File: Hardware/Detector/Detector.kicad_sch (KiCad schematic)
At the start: 0 parts

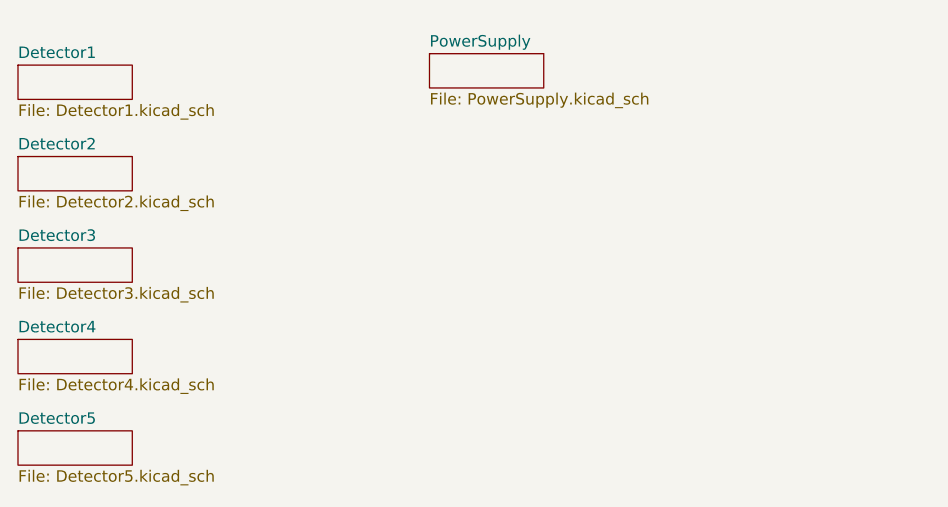
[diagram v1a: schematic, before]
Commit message: further implementation of low cost version
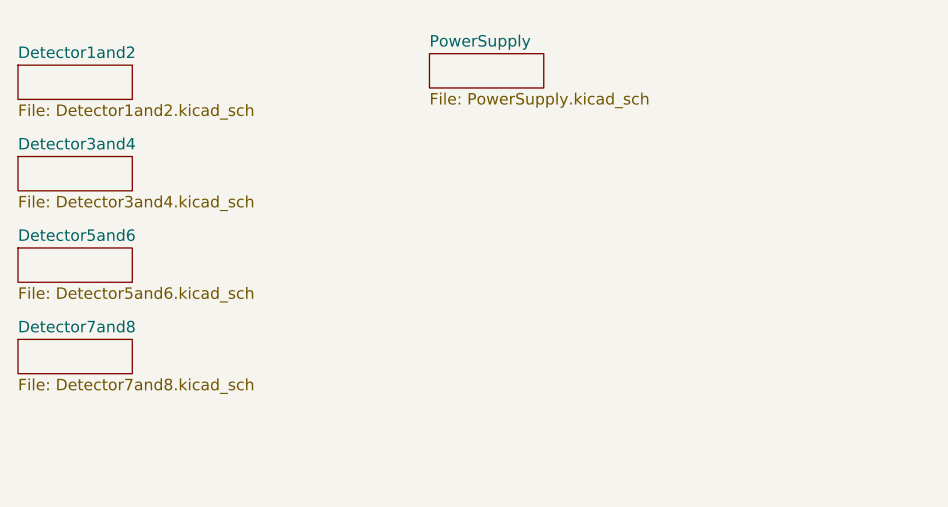
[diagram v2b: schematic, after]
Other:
- sheet Detector1 renamed Detector1and2
- sheet Detector2 renamed Detector3and4
- sheet Detector3 renamed Detector5and6
- sheet Detector4 renamed Detector7and8
- removed sheet Detector5
- sheet Detector1and2: file Detector1.kicad_sch -> Detector1and2.kicad_sch
- sheet Detector3and4: file Detector2.kicad_sch -> Detector3and4.kicad_sch
- sheet Detector5and6: file Detector3.kicad_sch -> Detector5and6.kicad_sch
- sheet Detector7and8: file Detector4.kicad_sch -> Detector7and8.kicad_sch

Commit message: fixed footprints, changed kicad scheet name, added a bit of decription to schematics
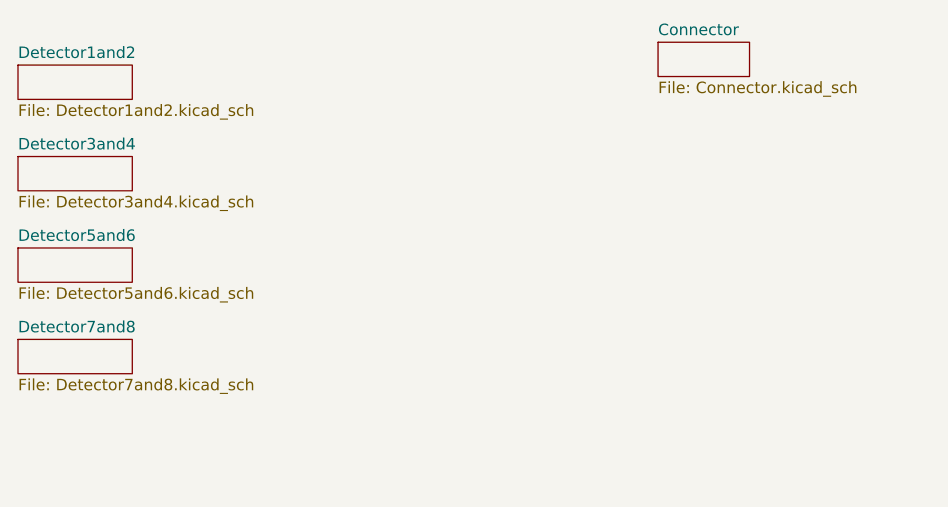
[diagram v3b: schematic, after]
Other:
- removed sheet PowerSupply
- added sheet Connector (Connector.kicad_sch)
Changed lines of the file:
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@@
 (kicad_sch (version 20210621) (generator eeschema)
   (paper "A4")
+  (sheet (at 132.08 43.18) (size 10.16 3.81) (fields_autoplaced)
+    (stroke (width 0.0006) (type solid) (color 0 0 0 0))
+    (fill (color 0 0 0 0.0000))
+    (property "Sheet name" "Connector" (id 0) (at 132.08 42.5443 0)
+      (effects (font (size 1.27 1.27)) (justify left bottom))
+    )
+    (property "Sheet file" "Connector.kicad_sch" (id 1) (at 132.08 47.4987 0)
+      (effects (font (size 1.27 1.27)) (justify left top))
+    )
+  )
   (sheet (at 60.96 45.72) (size 12.7 3.81) (fields_autoplaced)
     (stroke (width 0) (type solid) (color 0 0 0 0))
@@
     )
     (property "Sheet file" "Detector7and8.kicad_sch" (id 1) (at 60.96 80.5185 0)
-      (effects (font (size 1.27 1.27)) (justify left top))
-    )
-  )
-  (sheet (at 106.68 44.45) (size 12.7 3.81) (fields_autoplaced)
-    (stroke (width 0) (type solid) (color 0 0 0 0))
-    (fill (color 0 0 0 0.0000))
-    (property "Sheet name" "PowerSupply" (id 0) (at 106.68 43.8145 0)
-      (effects (font (size 1.27 1.27)) (justify left bottom))
-    )
-    (property "Sheet file" "PowerSupply.kicad_sch" (id 1) (at 106.68 48.7685 0)
       (effects (font (size 1.27 1.27)) (justify left top))
     )
@@
     (path "/00000000-0000-0000-0000-00006126c995" (page "4"))
     (path "/00000000-0000-0000-0000-00006126cbd6" (page "5"))
-    (path "/00000000-0000-0000-0000-0000613a12f3" (page "7"))
+    (path "/5f2e3474-4294-4ba3-9888-5e127036e05d" (page "7"))
   )
   (symbol_instances
@@
       (reference "#FLG01") (unit 1) (value "PWR_FLAG") (footprint "")
     )
-    (path "/00000000-0000-0000-0000-0000613a12f3/00000000-0000-0000-0000-0000613a2d09"
-      (reference "#FLG02") (unit 1) (value "PWR_FLAG") (footprint "")
-    )
-    (path "/00000000-0000-0000-0000-0000613a12f3/00000000-0000-0000-0000-0000613a2d03"
-      (reference "#FLG03") (unit 1) (value "PWR_FLAG") (footprint "")
-    )
-    (path "/00000000-0000-0000-0000-0000613a12f3/00000000-0000-0000-0000-0000613a2ce4"
-      (reference "#FLG04") (unit 1) (value "PWR_FLAG") (footprint "")
+    (path "/5f2e3474-4294-4ba3-9888-5e127036e05d/06133da6-7cc3-4082-a5f3-3c340855df19"
+      (reference "#FLG?") (unit 1) (value "PWR_FLAG") (footprint "")
+    )
+    (path "/5f2e3474-4294-4ba3-9888-5e127036e05d/853a2901-ebb3-4f30-bb7f-c3af7d416212"
+      (reference "#FLG?") (unit 1) (value "PWR_FLAG") (footprint "")
+    )
+    (path "/5f2e3474-4294-4ba3-9888-5e127036e05d/9d2454be-5e62-4368-82c6-b9619bf6d756"
+      (reference "#FLG?") (unit 1) (value "PWR_FLAG") (footprint "")
     )
     (path "/00000000-0000-0000-0000-00006126bc2d/00000000-0000-0000-0000-000061297e78"
@@
       (reference "#PWR019") (unit 1) (value "GND") (footprint "")
     )
-    (path "/00000000-0000-0000-0000-0000613a12f3/00000000-0000-0000-0000-0000613a2ceb"
-      (reference "#PWR020") (unit 1) (value "VCC") (footprint "")
-    )
-    (path "/00000000-0000-0000-0000-0000613a12f3/00000000-0000-0000-0000-0000613a2cf1"
-      (reference "#PWR021") (unit 1) (value "GND") (footprint "")
-    )
     (path "/00000000-0000-0000-0000-00006126bc2d/c606fb33-e83c-4379-997e-ae830a0633db"
       (reference "#PWR022") (unit 1) (value "GND") (footprint "")
@@
       (reference "#PWR026") (unit 1) (value "GND") (footprint "")
     )
+    (path "/5f2e3474-4294-4ba3-9888-5e127036e05d/c64404e3-c5a4-45e5-b3f5-f07ff96d3c86"
+      (reference "#PWR?") (unit 1) (value "GND") (footprint "")
+    )
+    (path "/5f2e3474-4294-4ba3-9888-5e127036e05d/f020742a-bb32-463f-a128-fd61cbeed9e0"
+      (reference "#PWR?") (unit 1) (value "VCC") (footprint "")
+    )
     (path "/00000000-0000-0000-0000-00006126bc2d/00000000-0000-0000-0000-000061297ddf"
       (reference "C1") (unit 1) (value "2p2") (footprint "Capacitor_SMD:C_0402_1005Metric")
@@
       (reference "R22") (unit 1) (value "10k") (footprint "Resistor_SMD:R_0402_1005Metric")
     )
-    (path "/00000000-0000-0000-0000-0000613a12f3/00000000-0000-0000-0000-00006158fd79"
-      (reference "TP1") (unit 1) (value "TestPoint") (footprint "TestPoint:TestPoint_THTPad_D2.5mm_Drill1.2mm")
-    )
-    (path "/00000000-0000-0000-0000-0000613a12f3/00000000-0000-0000-0000-0000615908a9"
-      (reference "TP2") (unit 1) (value "TestPoint") (footprint "TestPoint:TestPoint_THTPad_D2.5mm_Drill1.2mm")
-    )
-    (path "/00000000-0000-0000-0000-0000613a12f3/00000000-0000-0000-0000-000061592458"
-      (reference "TP3") (unit 1) (value "TestPoint") (footprint "TestPoint:TestPoint_THTPad_D2.5mm_Drill1.2mm")
+    (path "/5f2e3474-4294-4ba3-9888-5e127036e05d/80ad8886-8277-4b99-a3ab-d7372042ac3b"
+      (reference "TP?") (unit 1) (value "TestPoint") (footprint "TestPoint:TestPoint_THTPad_D2.5mm_Drill1.2mm")
+    )
+    (path "/5f2e3474-4294-4ba3-9888-5e127036e05d/cb6df753-a749-41d3-9c0d-94316f12f764"
+      (reference "TP?") (unit 1) (value "TestPoint") (footprint "TestPoint:TestPoint_THTPad_D2.5mm_Drill1.2mm")
+    )
+    (path "/5f2e3474-4294-4ba3-9888-5e127036e05d/d6e76c16-a992-4b76-9f80-139c651fa51d"
+      (reference "TP?") (unit 1) (value "TestPoint") (footprint "TestPoint:TestPoint_THTPad_D2.5mm_Drill1.2mm")
     )
     (path "/00000000-0000-0000-0000-00006126bc2d/016b2bd9-b16e-4b2a-8d92-eca9fb803dc8"
